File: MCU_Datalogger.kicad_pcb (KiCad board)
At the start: 2 copper layers, 29 parts, among them J1 Conn_01x04_Pin, J2 Conn_01x09_Pin, J3 Conn_01x04_Pin, J4 Conn_02x03_Odd_Even, U1 24LC1025, U2 DS1337S_, U3 24LC1025, U4 ATMEGA328P-AU, Y1 32.768 KHz, Y2 16 MHz

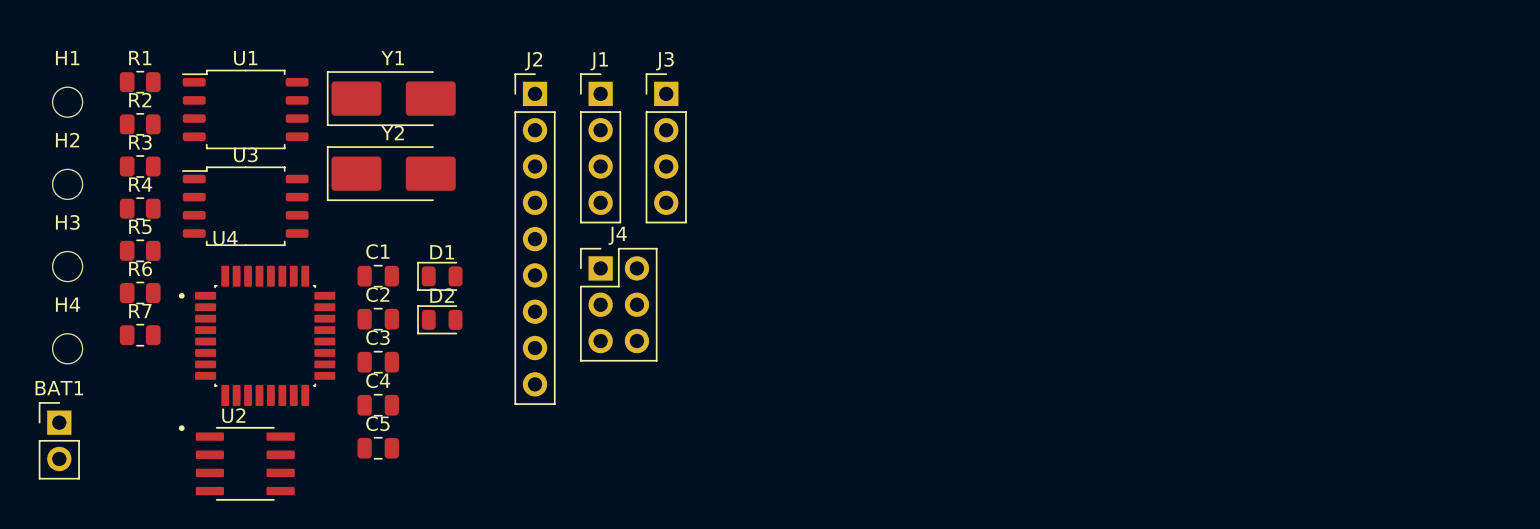
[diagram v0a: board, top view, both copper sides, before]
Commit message: Completed placement of footprints.
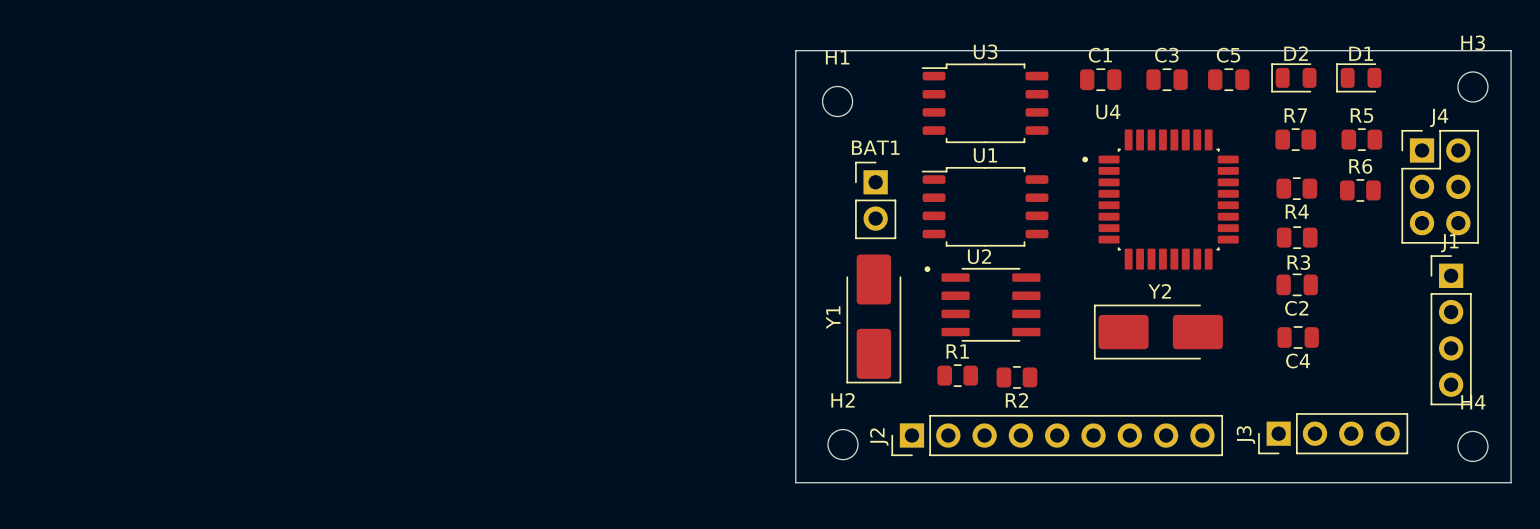
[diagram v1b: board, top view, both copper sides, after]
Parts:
- moved H3 99.1 mm to (183.1, 62.0)
- moved H4 98.6 mm to (183.1, 87.1)
- moved R5 85.8 mm to (175.4, 65.7)
- moved R6 85.7 mm to (175.3, 69.2)
- moved R7 82.0 mm to (170.7, 65.7)
- moved R3 81.1 mm to (170.8, 72.5), turned to 180 degrees
- moved R4 80.9 mm to (170.8, 69.1), turned to 180 degrees
- moved D1 65.8 mm to (175.3, 61.3)
- moved C5 64.9 mm to (166.1, 61.5)
- moved C4 64.5 mm to (170.9, 79.5), turned to 180 degrees
- moved C2 64.3 mm to (170.8, 75.8), turned to 180 degrees
- moved U4 63.9 mm to (161.8, 69.8)
- moved R2 63.8 mm to (151.2, 82.3), turned to 180 degrees
- moved D2 62.1 mm to (170.8, 61.3)
- moved J1 60.8 mm to (181.6, 75.2)
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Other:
- board outline added: 50 x 30.2 mm

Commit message: Routing sans GND VCC complete.
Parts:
- moved J1 1.40 mm to (183.0, 75.2)
- moved H1 1.02 mm to (138.7, 62.0)
- moved R6 0.90 mm to (175.7, 70.0)
- moved J4 0.89 mm to (180.5, 66.5)
- moved D1 0.89 mm to (175.8, 62.1)
- moved R5 0.85 mm to (175.7, 66.4), turned to 180 degrees
- moved R7 0.80 mm to (171.0, 66.4)
- moved D2 0.79 mm to (171.0, 62.1)
- moved U4 0.78 mm to (161.8, 70.6)
- moved R4 0.78 mm to (171.0, 69.8)
- moved C2 0.77 mm to (171.0, 76.6)
- moved R3 0.77 mm to (171.0, 73.3)
- moved BAT1 0.76 mm to (141.4, 69.4)
- moved J3 0.76 mm to (169.6, 87.0)
- moved R1 0.76 mm to (147.2, 82.9)
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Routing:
- net /VCC: track 0.00 -> 105.6 mm, vias 0 -> 1
- net /SCK: track 0.00 -> 99.7 mm, vias 0 -> 3
- net Net-(D2-A): track 0.00 -> 83.7 mm, vias 0 -> 6
- net /SDA: track 0.00 -> 57.1 mm, vias 0 -> 2
- net GND: track 0.00 -> 52.2 mm, vias 0 -> 6
- net /RX: track 0.00 -> 33.3 mm, vias 0 -> 1
- net /TX: track 0.00 -> 32.7 mm, vias 0 -> 1
- net /RESET: track 0.00 -> 28.1 mm, vias 0 -> 2
- net /D2: track 0.00 -> 26.8 mm, vias 0 -> 1
- net /D3: track 0.00 -> 26.2 mm
- net Net-(U4-PB7): track 0.00 -> 26.2 mm, vias 0 -> 2
- net /MOSI: track 0.00 -> 23.8 mm
- net /D4: track 0.00 -> 23.2 mm
- net Net-(U4-PB6): track 0.00 -> 22.6 mm
- net /MISO: track 0.00 -> 19.3 mm, vias 0 -> 1
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
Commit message: Completed routing.
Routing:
- net GND: track 52.2 -> 119.8 mm, vias 6 -> 12
- net /VCC: track 105.6 -> 117.9 mm
- net /D4: track 23.2 -> 31.1 mm
- net /D3: track 26.2 -> 32.8 mm
- net /SCK: track 99.7 -> 106.3 mm
- net Net-(U4-AREF): track 14.8 -> 17.5 mm
- net /RX: track 33.3 -> 30.7 mm
- net /SDA: track 57.1 -> 58.4 mm
- net /TX: track 32.7 -> 31.7 mm
- added copper zone on F.Cu, net /VCC
- added copper zone on B.Cu, net GND

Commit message: Completed the Design.
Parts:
- added REF**: KiCad-Logo2_5mm_SilkScreen, Symbol:KiCad-Logo2_5mm_SilkScreen, B.Cu at (161.0, 81.0)
- renumbered BAT1 to BAT
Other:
- board text added: "2"
- board text added: "2layer_MCU_Datalogger - 2Mbit EEPROM - RTC - I2C, SPI, GPIOs Version 1.0"
- board text added: "3"
- board text added: "4"
- board text added: "5"
- board text added: "6"
- board text added: "7"
- board text added: "8"
- board text added: "CWL_Company"
- board text added: "GND"
- board text added: "GPIO"
- board text added: "I2C"
- board text added: "ICSP"
- board text added: "ICSP MISO|VCC SCK |MOSI RST |GND"
- board text added: "RX"
- board text added: "SCK"
- board text added: "SDA"
- board text added: "SERIAL"
- board text added: "TX"
- board text added: "VCC"

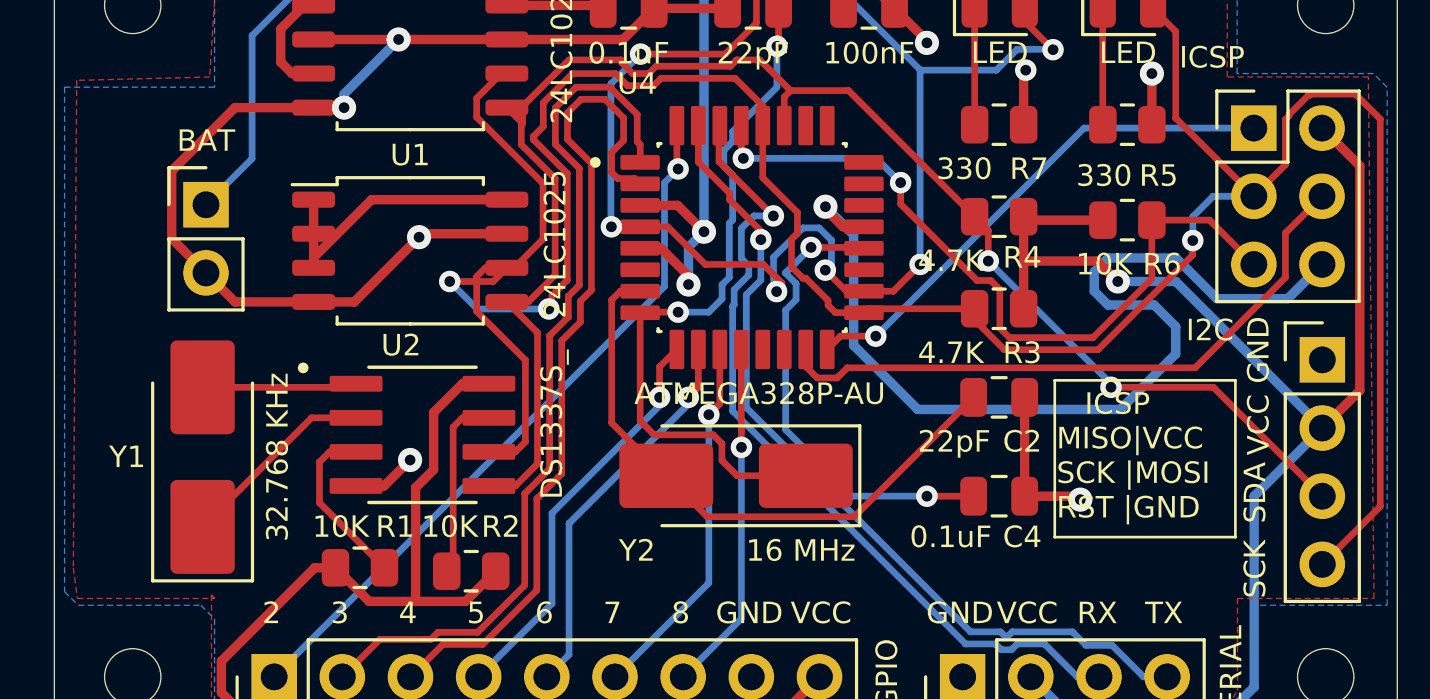
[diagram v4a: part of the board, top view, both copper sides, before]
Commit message: Completed 2-layer PCB project.
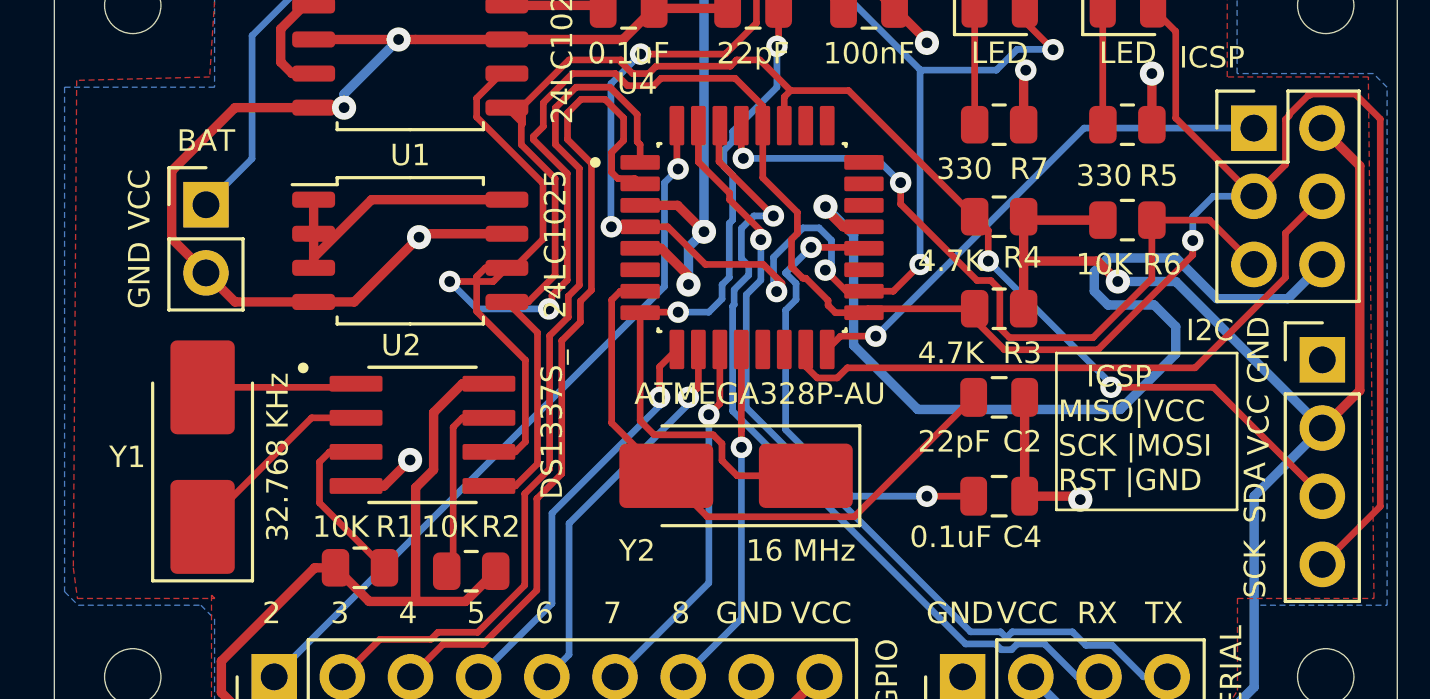
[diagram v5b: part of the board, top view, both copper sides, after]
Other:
- board text added: "0.0000 mm / 0.0000 mm"
- board text added: "0.3000 mm"
- board text added: "1.6000 mm"
- board text added: "50.0380 mm x 30.2260 mm"
- board text added: "None"
- board text added: "구리 레이어 수:"
- board text added: "구리 마감:"
- board text added: "기판 특성"
- board text added: "도금된 보드 가장자리:"
- board text added: "보드 두께:"
- board text added: "보드 전체 치수 :"
- board text added: "성곽 패드:"
- board text added: "아니오"
- board text added: "에지 카드 커넥터:"
- board text added: "임피던스 제어:"
- board text added: "최소 배선/간격:"
- board text added: "최소 홀 직경:"
